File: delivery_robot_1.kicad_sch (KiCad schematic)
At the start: 46 parts, among them J1 SWD, J2 Conn_01x02, J3 UART, J4 BOOT0 jumper, SW1 RESET, U1 STM32F091RCTx, U2 PTPSM63606RDLR, U3 TPS54202DDCR, Y3 Crystal_GND24

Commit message: Select optional STM32 HSE crystal and matching load capacitors
Specify Y3 as Abracon ABM3B-8.000MHZ-B2-T and C5/C6 as Murata
GRM1885C1H160JA01D (16 pF, 50 V, C0G, 5%). Retain DNP on all three
so initial assembly can use the MCU internal clock while preserving
pads and purchasing information for a later external-clock option.

STM32F091xB/xC datasheet DocID026284 Rev 4, p69 Table 39, permits
8 MHz HSE and gives 10 mA/V minimum startup transconductance. Its
rough 10 pF pin/board capacitance estimate yields two 16 pF caps
for the crystal's 18 pF load. ST AN2867 sections 3.3-3.5 give a
calculated startup gain margin of 7.92, exceeding the recommended 5.

Abracon ABM3B Rev U p3 verifies the standard KiCad four-pad footprint:
1.8 x 1.2 mm lands on 4.0 x 2.4 mm centers, with ground pins 2/4.
Murata reference sheet 01A p27 Table 2 supports project-local capacitor
lands of 0.65 x 0.70 mm with a 0.70 mm gap. Document layout, firmware,
load tuning and crystal drive/startup checks still required on hardware.

Sources:
https://www.st.com/resource/en/datasheet/stm32f091rc.pdf
https://www.st.com/resource/en/application_note/cd00221665-oscillator-design-guide-for-stm8af-al-s-stm32-mcus-and-mpus-stmicroelectronics.pdf
https://abracon.com/Resonators/abm3b.pdf
https://search.murata.co.jp/Ceramy/image/img/A01X/G101/ENG/GRM1885C1H160JA01-01A.pdf

Validation: exported component-pin net sets are unchanged; pcbnew
confirms land geometry and pin numbering. Existing unrelated KiCad
viewer serialization changes are left unstaged.
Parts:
- C5, C6: value C -> 16pF; footprint (none) -> project_footprints:C_Murata_GRM1885C1H160JA01; MPN (none) -> GRM1885C1H160JA01D; Manufacturer (none) -> Murata; Specification (none) -> 16pF / 50V C0G / 5%
- Y3: value Crystal_GND24 -> 8MHz; footprint (none) -> Crystal:Crystal_SMD_Abracon_ABM3B-4Pin_5.0x3.2mm; MPN (none) -> ABM3B-8.000MHZ-B2-T; Manufacturer (none) -> Abracon; Specification (none) -> 8MHz / CL=18pF / ESR<=200 ohm
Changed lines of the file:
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@@
 			)
 		)
-		(property "Value" "Crystal_GND24"
+		(property "Value" "8MHz"
 			(at 54.61 90.0998 0)
 			(show_name no)
@@
 			)
 		)
-		(property "Footprint" ""
+		(property "Footprint" "Crystal:Crystal_SMD_Abracon_ABM3B-4Pin_5.0x3.2mm"
 			(at 43.18 93.98 0)
 			(hide yes)
@@
 			)
 		)
-		(property "Datasheet" ""
+		(property "Datasheet" "https://abracon.com/Resonators/abm3b.pdf"
 			(at 43.18 93.98 0)
 			(hide yes)
@@
 		)
 		(property "Description" "Four pin crystal, GND on pins 2 and 4"
+			(at 43.18 93.98 0)
+			(hide yes)
+			(show_name no)
+			(do_not_autoplace no)
+			(effects
+				(font
+					(size 1.27 1.27)
+				)
+			)
+		)
+		(property "Manufacturer" "Abracon"
+			(at 43.18 93.98 0)
+			(hide yes)
+			(show_name no)
+			(do_not_autoplace no)
+			(effects
+				(font
+					(size 1.27 1.27)
+				)
+			)
+		)
+		(property "MPN" "ABM3B-8.000MHZ-B2-T"
+			(at 43.18 93.98 0)
+			(hide yes)
+			(show_name no)
+			(do_not_autoplace no)
+			(effects
+				(font
+					(size 1.27 1.27)
+				)
+			)
+		)
+		(property "Specification" "8MHz / CL=18pF / ESR<=200 ohm"
 			(at 43.18 93.98 0)
 			(hide yes)
@@
 			)
 		)
-		(property "Value" "C"
+		(property "Value" "16pF"
 			(at 38.1 102.8699 0)
 			(show_name no)
@@
 			)
 		)
-		(property "Footprint" ""
+		(property "Footprint" "project_footprints:C_Murata_GRM1885C1H160JA01"
 			(at 35.2552 105.41 0)
 			(hide yes)
@@
 			)
 		)
-		(property "Datasheet" ""
+		(property "Datasheet" "https://search.murata.co.jp/Ceramy/image/img/A01X/G101/ENG/GRM1885C1H160JA01-01A.pdf"
 			(at 34.29 101.6 0)
 			(hide yes)
@@
 		)
 		(property "Description" "Unpolarized capacitor"
+			(at 34.29 101.6 0)
+			(hide yes)
+			(show_name no)
+			(do_not_autoplace no)
+			(effects
+				(font
+					(size 1.27 1.27)
+				)
+			)
+		)
+		(property "Manufacturer" "Murata"
+			(at 34.29 101.6 0)
+			(hide yes)
+			(show_name no)
+			(do_not_autoplace no)
+			(effects
+				(font
+					(size 1.27 1.27)
+				)
+			)
+		)
+		(property "MPN" "GRM1885C1H160JA01D"
+			(at 34.29 101.6 0)
+			(hide yes)
+			(show_name no)
+			(do_not_autoplace no)
+			(effects
+				(font
+					(size 1.27 1.27)
+				)
+			)
+		)
+		(property "Specification" "16pF / 50V C0G / 5%"
 			(at 34.29 101.6 0)
 			(hide yes)
@@
 			)
 		)
-		(property "Value" "C"
+		(property "Value" "16pF"
 			(at 54.61 102.8699 0)
 			(show_name no)
@@
 			)
 		)
-		(property "Footprint" ""
+		(property "Footprint" "project_footprints:C_Murata_GRM1885C1H160JA01"
 			(at 51.7652 105.41 0)
 			(hide yes)
@@
 			)
 		)
-		(property "Datasheet" ""
+		(property "Datasheet" "https://search.murata.co.jp/Ceramy/image/img/A01X/G101/ENG/GRM1885C1H160JA01-01A.pdf"
 			(at 50.8 101.6 0)
 			(hide yes)
@@
 			(at 50.8 101.6 0)
 			(hide yes)
+			(show_name no)
+			(do_not_autoplace no)
+			(effects
+				(font
+					(size 1.27 1.27)
+				)
+			)
+		)
+		(property "Manufacturer" "Murata"
+			(at 50.8 101.6 0)
+			(hide yes)
+			(show_name no)
+			(do_not_autoplace no)
+			(effects
+				(font
+					(size 1.27 1.27)
+				)
+			)
+		)
+		(property "MPN" "GRM1885C1H160JA01D"
+			(at 50.8 101.6 0)
+			(hide yes)
+			(show_name no)
+			(do_not_autoplace no)
+			(effects
+				(font
+					(size 1.27 1.27)
+				)
+			)
+		)
+		(property "Specification" "16pF / 50V C0G / 5%"
+			(at 50.8 101.6 0)
+			(hide yes)

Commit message: Select replaceable 7.5 A battery-input fuse and verified MINI holder
Specify F1 as a Keystone 3568 PCB holder with a Littelfuse 029707.5L
7.5 A, 32 VDC MINI insert. Both bucks share this input branch: their
5 V/6 A and 5 V/2 A outputs total 40 W. At the battery's 10.8 V minimum
normal voltage and an assumed 85% efficiency, estimated input current
is 4.36 A. The LDO load is already included in the 2 A branch.

Littelfuse MINI 32 V datasheet (2024-09-27), p3, allows 6.0 A at 40 C
for the 7.5 A fuse versus 4.0 A for the 5 A fuse. This makes 7.5 A the
lowest standard option above the estimated continuous full-load current
at the team's 40 C ambient limit. Pages 1-2 specify 32 VDC operation
and 1000 A interruption at 32 VDC, with normal battery voltage <=14.6 V.
These ratings do not establish actual battery short-circuit current.

Keystone drawing 3568 Rev E (2023-05-17) specifies four mounting holes
on 9.92 x 3.40 mm centers and 1.60 mm minimum hole diameter. The standard
KiCad Fuseholder_Blade_Mini_Keystone_3568 footprint matches the spacing
and uses 1.78 mm holes with 2.78 mm copper pads. Repeated pad numbers
correctly map two leads per contact to the fuse symbol's two terminals.
Keystone explicitly lists compatibility with Littelfuse 297 MINI fuses.
Use a replaceable holder for service without soldering a replacement fuse.

Record holder and insert as separate purchasing items: main MPN 3568
identifies the PCB-mounted part; FuseMPN 029707.5L identifies the insert.
Document both quantities and BOM-export requirements to avoid omitting
the fuse. Retain F1 populated and preserve Y3/C5/C6 DNP flags.

Sources:
https://www.littelfuse.com/assetdocs/littelfuse-datasheet-297-mini32v?assetguid=42c9dd21-a88e-4328-8e67-2f832444faf1
https://www.keyelco.com/product.cfm/product_id/306
https://www.keyelco.com/product-pdf.cfm?p=306

Validation: exported component-pin net sets are unchanged; only F1
component metadata/value/footprint changed. pcbnew confirms holder
pad geometry. ERC r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
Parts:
- F1: value Fuse -> 7.5A / 32VDC; footprint (none) -> Fuse:Fuseholder_Blade_Mini_Keystone_3568; AssemblyBOM (none) -> 1x Keystone 3568 holder + 1x Littelfuse 029707.5L fuse; ord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; FuseDatasheet (none) -> https://www.littelfuse.com/assetdocs/littelfuse-datasheet-2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; FuseMPN (none) -> 029707.5L; FuseManufacturer (none) -> Littelfuse; MPN (none) -> 3568; Manufacturer (none) -> Keystone Electronics; Specification (none) -> MINI holder with 7.5A / 32VDC fuse; 1000A DC interrupt rati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
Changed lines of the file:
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@@
 			)
 		)
-		(property "Value" "Fuse"
+		(property "Value" "7.5A / 32VDC"
 			(at 40.64 163.83 90)
 			(show_name no)
@@
 			)
 		)
-		(property "Footprint" ""
+		(property "Footprint" "Fuse:Fuseholder_Blade_Mini_Keystone_3568"
 			(at 40.64 165.862 90)
 			(hide yes)
@@
 			)
 		)
-		(property "Datasheet" ""
+		(property "Datasheet" "https://www.keyelco.com/product-pdf.cfm?p=306"
 			(at 40.64 167.64 0)
 			(hide yes)
@@
 			)
 		)
-		(property "Description" "Fuse"
+		(property "Description" "Replaceable MINI fuse assembly: Keystone 3568 holder and Littelfuse 029707.5L fuse"
 			(at 40.64 167.64 0)
 			(hide yes)
+			(show_name no)
+			(do_not_autoplace no)
+			(effects
+				(font
+					(size 1.27 1.27)
+				)
+			)
+		)
+		(property "Manufacturer" "Keystone Electronics"
+			(at 40.64 167.64 0)
+			(hide yes)
+			(show_name no)
+			(do_not_autoplace no)
+			(effects
+				(font
+					(size 1.27 1.27)
+				)
+			)
+		)
+		(property "MPN" "3568"
+			(at 40.64 167.64 0)
+			(hide yes)
+			(show_name no)
+			(do_not_autoplace no)
+			(effects
+				(font
+					(size 1.27 1.27)
+				)
+			)
+		)
+		(property "Specification" "MINI holder with 7.5A / 32VDC fuse; 1000A DC interrupt rating belongs to fuse"
+			(at 40.64 167.64 0)
+			(hide yes)
+			(show_name no)
+			(do_not_autoplace no)
+			(effects
+				(font
+					(size 1.27 1.27)
+				)
+			)
+		)
+		(property "FuseManufacturer" "Littelfuse"
+			(at 40.64 167.64 0)
+			(hide yes)
+			(show_name no)
+			(do_not_autoplace no)
+			(effects
+				(font
+					(size 1.27 1.27)
+				)
+			)
+		)
+		(property "FuseMPN" "029707.5L"
+			(at 40.64 167.64 0)
+			(hide yes)
+			(show_name no)
+			(do_not_autoplace no)
+			(effects
+				(font
+					(size 1.27 1.27)
+				)
+			)
+		)
+		(property "FuseDatasheet" "https://www.littelfuse.com/assetdocs/littelfuse-datasheet-297-mini32v?assetguid=42c9dd21-a88e-4328-8e67-2f832444faf1"
+			(at 40.64 167.64 0)
+			(hide yes)
+			(show_name no)
+			(do_not_autoplace no)
+			(effects
+				(font
+					(size 1.27 1.27)
+				)
+			)
+		)
+		(property "AssemblyBOM" "1x Keystone 3568 holder + 1x Littelfuse 029707.5L fuse; order both"
+			(at 40.64 167.64 0)
+			(hide yes)

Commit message: testinggg
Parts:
- added D1: D_Capacitance, symbol Device:D_Capacitance

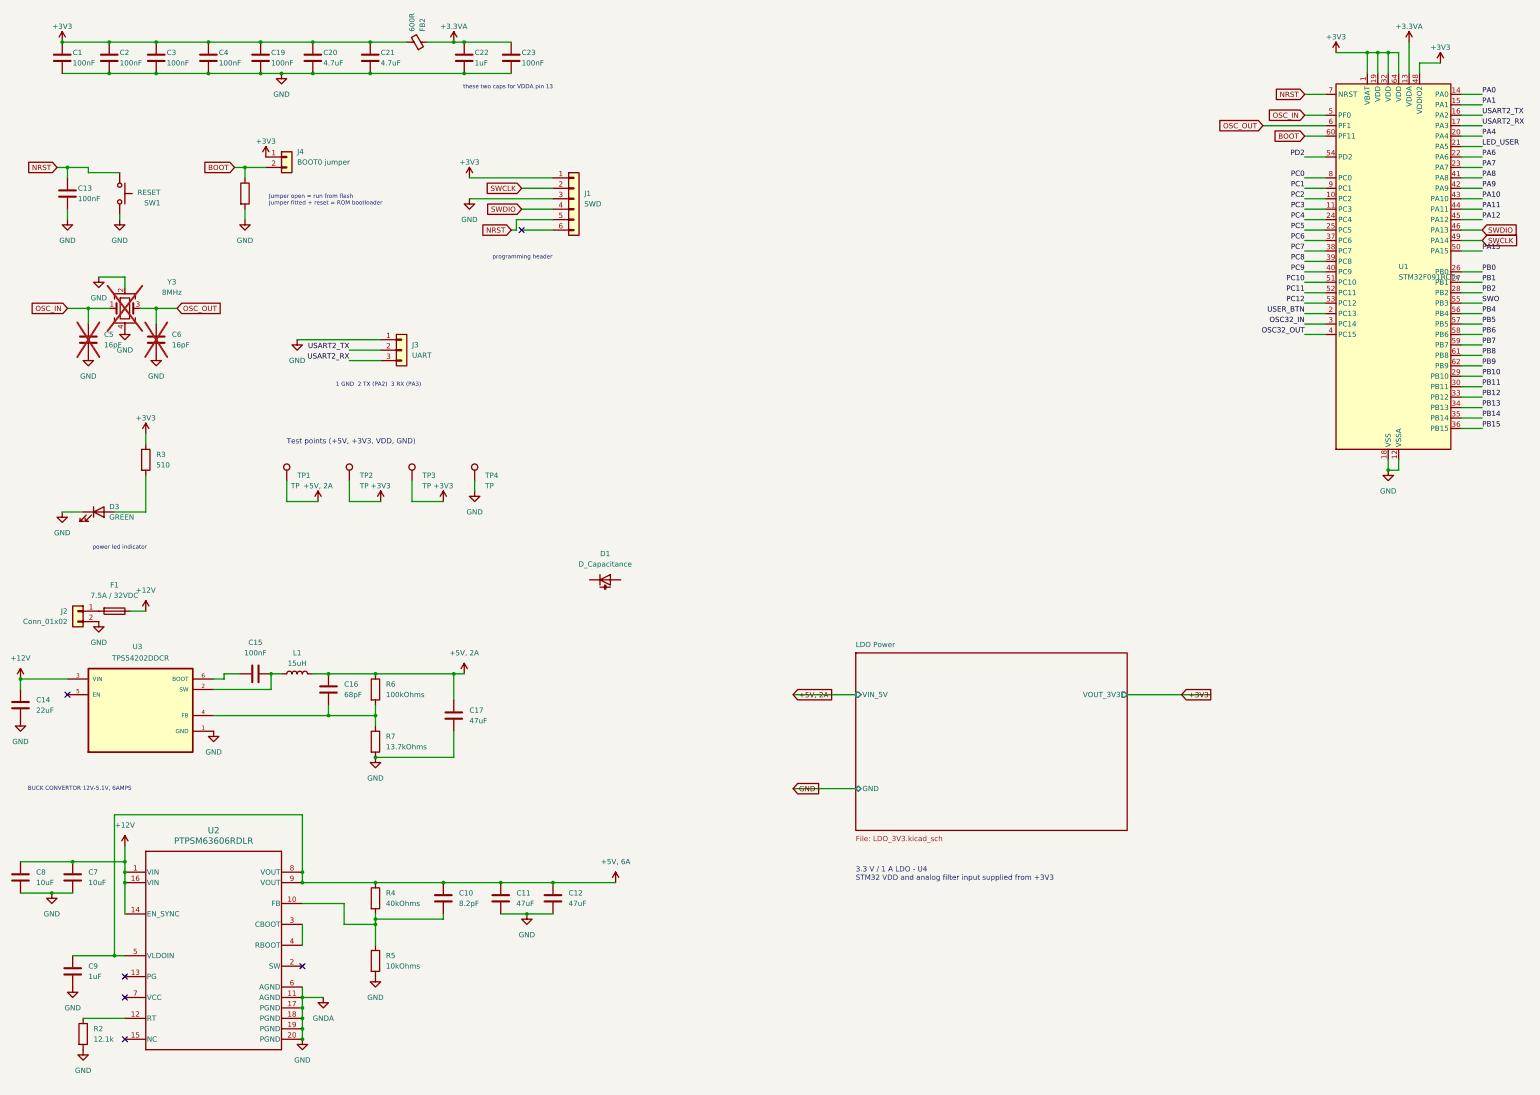
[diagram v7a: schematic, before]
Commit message: Move both buck converters onto hierarchical sheets
Split the TPS54202 (U3) and TPSM63606 (U2) circuits out of the root
schematic into Buck_5V_2A and Buck_5V_6A child sheets, wired like the
LDO sheet with VIN_12V, GND and VOUT_5V hierarchical labels connected
to +12V, GND, +5V 2A and +5V 6A in the root. Net connectivity is
unchanged except the redundant GNDA symbol on U2 is dropped.

Add datasheet, product page, key specs and design notes to U2 and U3,
and document the sheet layout and open design checks in README and
docs/power-supply.md.
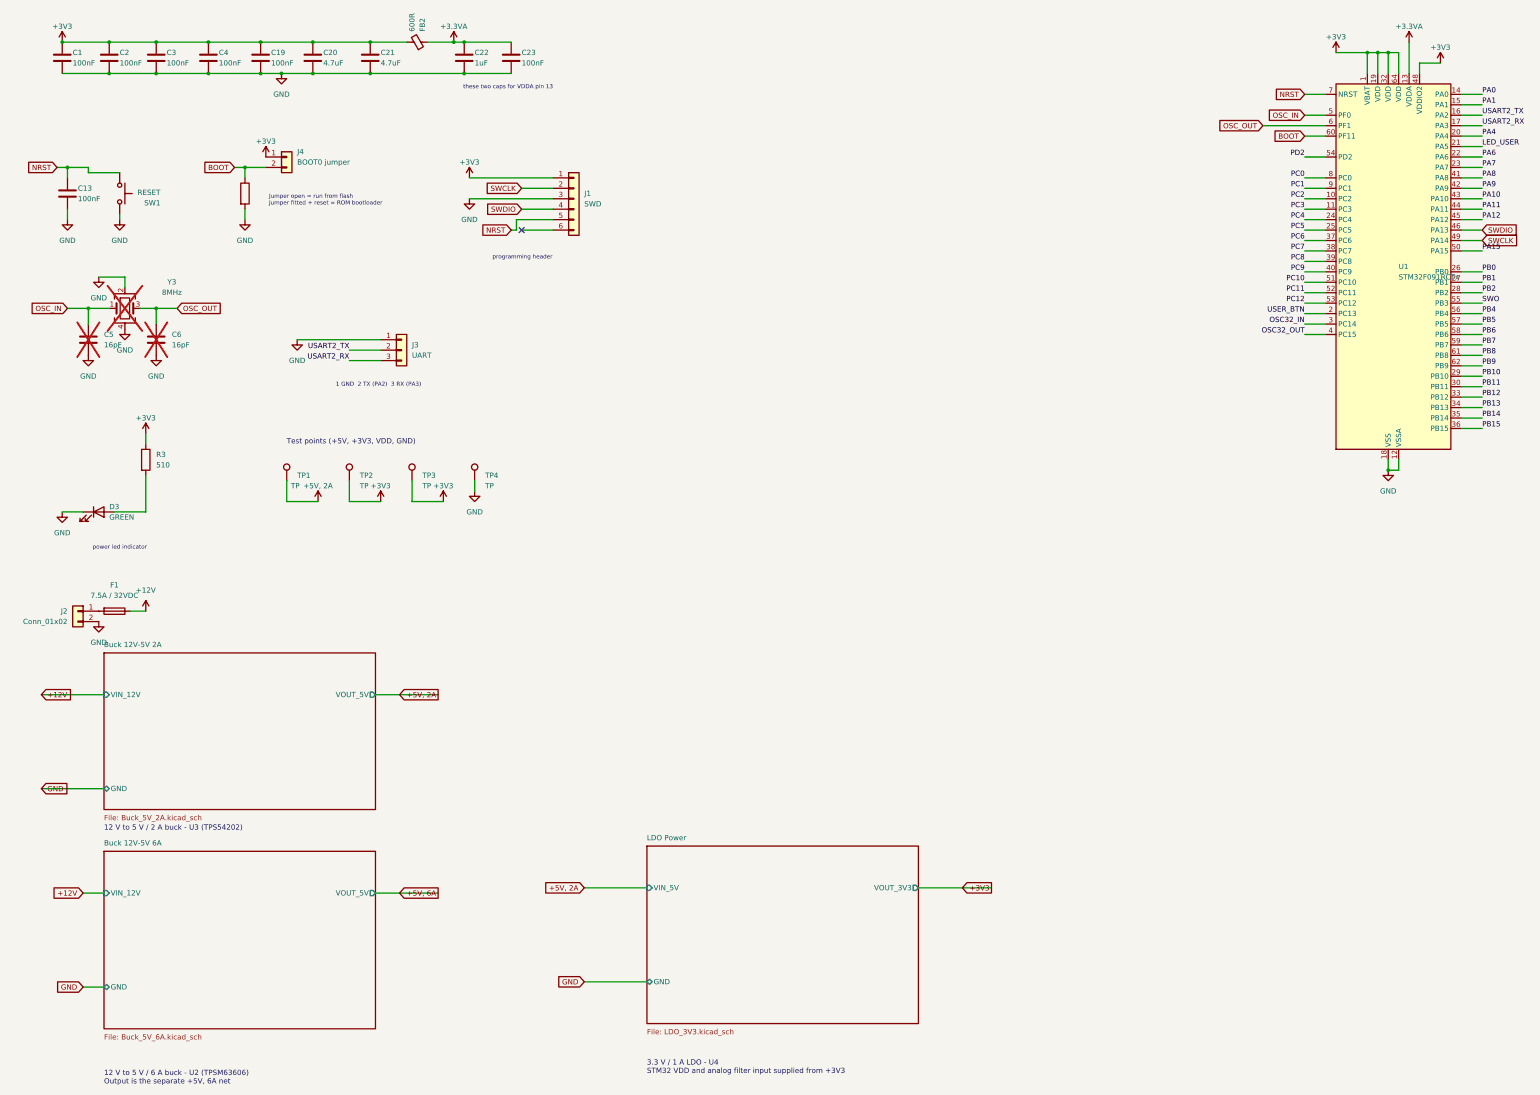
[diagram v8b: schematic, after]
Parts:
- removed C10: 8.2pF, Capacitor_SMD:C_0603_1608Metric, symbol Device:C
- removed C11, C12, C17: 47uF, project_footprints:C_Murata_GRM32ER71A476ME15, symbol Device:C
- removed C14: 22uF, project_footprints:C_TDK_C5750X7R1H226M250KB, symbol Device:C
- removed C15: 100nF, Capacitor_SMD:C_0603_1608Metric, symbol Device:C
- removed C16: 68pF, Capacitor_SMD:C_0603_1608Metric, symbol Device:C
- removed C7, C8: 10uF, Capacitor_SMD:C_1210_3225Metric, symbol Device:C
- removed C9: 1uF, Capacitor_SMD:C_0603_1608Metric, symbol Device:C
- removed D1: D_Capacitance, symbol Device:D_Capacitance
- removed L1: 15uH, Inductor_SMD:L_Coilcraft_XAL6060-XXX, symbol Device:L
- removed R2: 12.1k, Resistor_SMD:R_0805_2012Metric, symbol Device:R
- removed R4: 40kOhms, Resistor_SMD:R_0805_2012Metric, symbol Device:R
- removed R5: 10kOhms, Resistor_SMD:R_0805_2012Metric, symbol Device:R
- removed R6: 100kOhms, Resistor_SMD:R_0805_2012Metric, symbol Device:R
- removed R7: 13.7kOhms, Resistor_SMD:R_0805_2012Metric, symbol Device:R
- removed U2: PTPSM63606RDLR, project_footprints:RDL0020A-MFG, symbol TPSM63606RDLR:PTPSM63606RDLR
- removed U3: TPS54202DDCR, project_footprints:SOT95P280X110-6N, symbol TPS54202DDCR:TPS54202DDCR
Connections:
- no-connect marks 6 -> 1
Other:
- added sheet Buck 12V-5V 2A (Buck_5V_2A.kicad_sch)
- added sheet Buck 12V-5V 6A (Buck_5V_6A.kicad_sch)
- note added: "12 V to 5 V / 2 A buck - U3 (TPS54202)"
- note added: "12 V to 5 V / 6 A buck - U2 (TPSM63606) Output is the separate +5V, 6A net"
- note removed: "BUCK CONVERTOR 12V-5.1V, 6AMPS"
